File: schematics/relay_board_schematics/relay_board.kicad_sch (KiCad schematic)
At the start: 45 parts, among them J1 Programming Header, P1 ACT_PWR, P2 ACT_PWR, P3 ACTUATOR, Q1 MMBF170, Q2 MMBF170, SW1 SW_DIP_x04, U1 SPST_POWER_RELAY, U2 PIC16F1826-ISO, U3 dpdt_relay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

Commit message: first attempt at rerouting
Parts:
- D1: footprint Diode_SMD:D_SMB_Handsoldering -> Diode_THT:D_DO-35_SOD27_P7.62mm_Horizontal
- TP0, TP1, TP2, TP3: footprint TestPoint:TestPoint_Loop_D2.50mm_Drill1.0mm_LowProfile -> custom:Socket_Strip_Straight_1x01_Pitch2.54mm
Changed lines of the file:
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@@
     (property "Reference" "TP2" (id 0) (at 217.17 34.798 0))
     (property "Value" "TEST_1P" (id 1) (at 217.17 33.02 0))
-    (property "Footprint" "TestPoint:TestPoint_Loop_D2.50mm_Drill1.0mm_LowProfile" (id 2) (at 212.09 27.94 0)
+    (property "Footprint" "custom:Socket_Strip_Straight_1x01_Pitch2.54mm" (id 2) (at 212.09 27.94 0)
       (effects (font (size 1.27 1.27)) hide)
     )
@@
     (property "Reference" "TP1" (id 0) (at 203.2 34.798 0))
     (property "Value" "TEST_1P" (id 1) (at 203.2 33.02 0))
-    (property "Footprint" "TestPoint:TestPoint_Loop_D2.50mm_Drill1.0mm_LowProfile" (id 2) (at 198.12 27.94 0)
+    (property "Footprint" "custom:Socket_Strip_Straight_1x01_Pitch2.54mm" (id 2) (at 198.12 27.94 0)
       (effects (font (size 1.27 1.27)) hide)
     )
@@
     (property "Reference" "TP0" (id 0) (at 189.23 19.812 0))
     (property "Value" "TEST_1P" (id 1) (at 189.23 21.59 0))
-    (property "Footprint" "TestPoint:TestPoint_Loop_D2.50mm_Drill1.0mm_LowProfile" (id 2) (at 194.31 26.67 0)
+    (property "Footprint" "custom:Socket_Strip_Straight_1x01_Pitch2.54mm" (id 2) (at 194.31 26.67 0)
       (effects (font (size 1.27 1.27)) hide)
     )
@@
     (property "Reference" "D1" (id 0) (at 102.87 118.11 0))
     (property "Value" "D" (id 1) (at 97.79 118.11 0))
-    (property "Footprint" "Diode_SMD:D_SMB_Handsoldering" (id 2) (at 100.33 118.11 0)
+    (property "Footprint" "Diode_THT:D_DO-35_SOD27_P7.62mm_Horizontal" (id 2) (at 100.33 118.11 0)
       (effects (font (size 1.27 1.27)) hide)
     )
@@
     (property "Reference" "TP3" (id 0) (at 143.51 124.46 0))
     (property "Value" "TEST_1P" (id 1) (at 144.78 121.92 0))
-    (property "Footprint" "TestPoint:TestPoint_Loop_D2.50mm_Drill1.0mm_LowProfile" (id 2) (at 134.62 118.11 0)
+    (property "Footprint" "custom:Socket_Strip_Straight_1x01_Pitch2.54mm" (id 2) (at 134.62 118.11 0)
       (effects (font (size 1.27 1.27)) hide)
     )
@@
     )
     (path "/00000000-0000-0000-0000-00005dfd5087"
-      (reference "D1") (unit 1) (value "D") (footprint "Diode_SMD:D_SMB_Handsoldering")
+      (reference "D1") (unit 1) (value "D") (footprint "Diode_THT:D_DO-35_SOD27_P7.62mm_Horizontal")
     )
     (path "/00000000-0000-0000-0000-00005dfd508d"
@@
     )
     (path "/00000000-0000-0000-0000-0000597cb866"
-      (reference "TP0") (unit 1) (value "TEST_1P") (footprint "TestPoint:TestPoint_Loop_D2.50mm_Drill1.0mm_LowProfile")
+      (reference "TP0") (unit 1) (value "TEST_1P") (footprint "custom:Socket_Strip_Straight_1x01_Pitch2.54mm")
     )
     (path "/00000000-0000-0000-0000-0000597cb649"
-      (reference "TP1") (unit 1) (value "TEST_1P") (footprint "TestPoint:TestPoint_Loop_D2.50mm_Drill1.0mm_LowProfile")
+      (reference "TP1") (unit 1) (value "TEST_1P") (footprint "custom:Socket_Strip_Straight_1x01_Pitch2.54mm")
     )
     (path "/00000000-0000-0000-0000-0000597cb557"
-      (reference "TP2") (unit 1) (value "TEST_1P") (footprint "TestPoint:TestPoint_Loop_D2.50mm_Drill1.0mm_LowProfile")
+      (reference "TP2") (unit 1) (value "TEST_1P") (footprint "custom:Socket_Strip_Straight_1x01_Pitch2.54mm")
     )
     (path "/00000000-0000-0000-0000-00005e14f9f3"
-      (reference "TP3") (unit 1) (value "TEST_1P") (footprint "TestPoint:TestPoint_Loop_D2.50mm_Drill1.0mm_LowProfile")
+      (reference "TP3") (unit 1) (value "TEST_1P") (footprint "custom:Socket_Strip_Straight_1x01_Pitch2.54mm")
     )
     (path "/00000000-0000-0000-0000-00005dfd4fdd"

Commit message: addressed Jack's comments on pcb
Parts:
- D1: footprint Diode_THT:D_DO-35_SOD27_P7.62mm_Horizontal -> Diode_SMD:D_SMB_Handsoldering
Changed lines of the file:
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@@
     (property "Reference" "D1" (id 0) (at 102.87 118.11 0))
     (property "Value" "D" (id 1) (at 97.79 118.11 0))
-    (property "Footprint" "Diode_THT:D_DO-35_SOD27_P7.62mm_Horizontal" (id 2) (at 100.33 118.11 0)
+    (property "Footprint" "Diode_SMD:D_SMB_Handsoldering" (id 2) (at 100.33 118.11 0)
       (effects (font (size 1.27 1.27)) hide)
     )
@@
     )
     (path "/00000000-0000-0000-0000-00005dfd5087"
-      (reference "D1") (unit 1) (value "D") (footprint "Diode_THT:D_DO-35_SOD27_P7.62mm_Horizontal")
+      (reference "D1") (unit 1) (value "D") (footprint "Diode_SMD:D_SMB_Handsoldering")
     )
     (path "/00000000-0000-0000-0000-00005dfd508d"

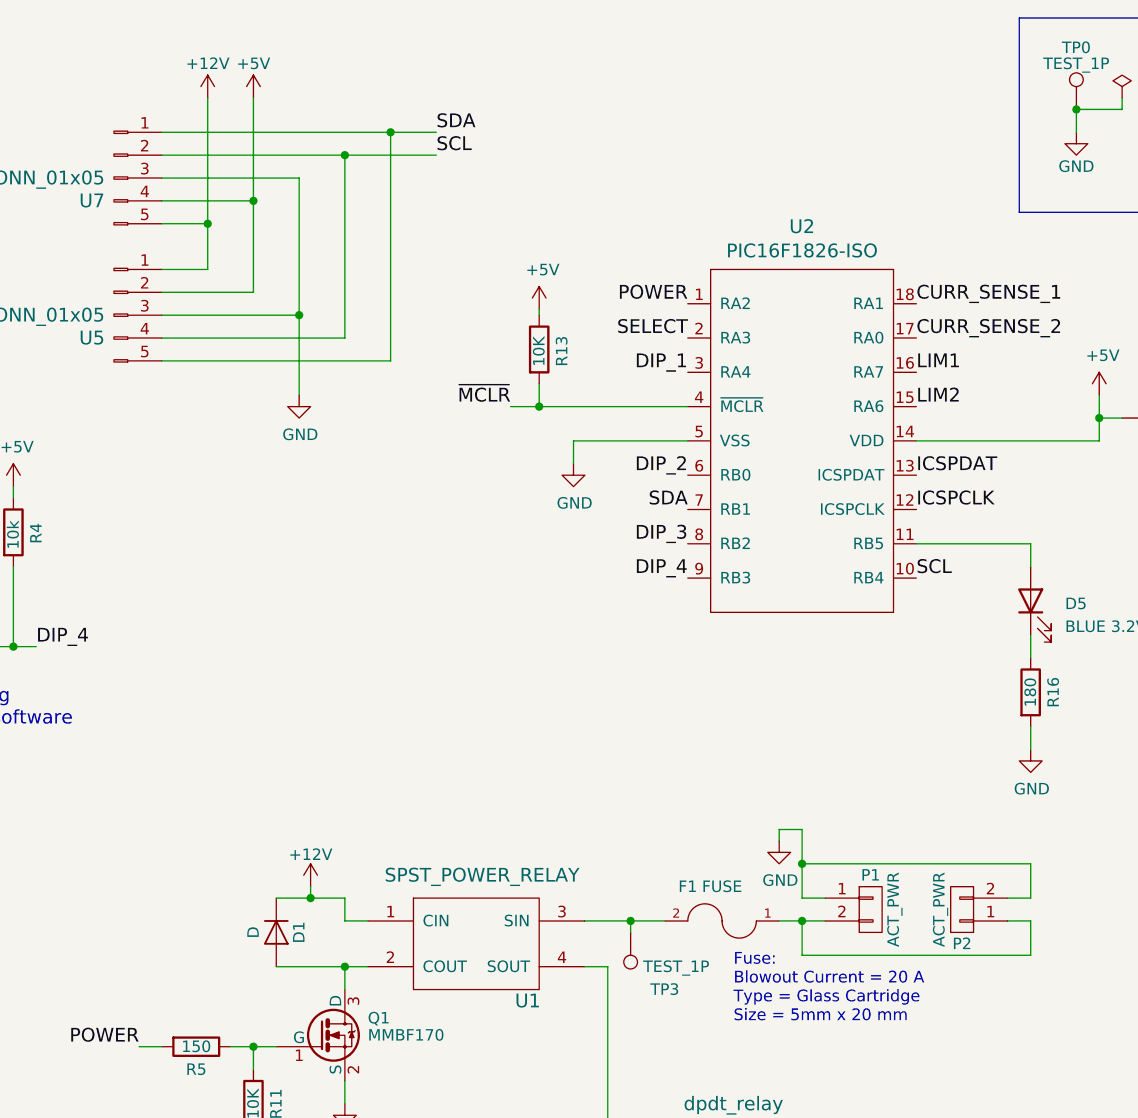
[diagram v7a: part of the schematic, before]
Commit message: Reversed the 5-pin and 2-pin screw terminals to match CAN support board
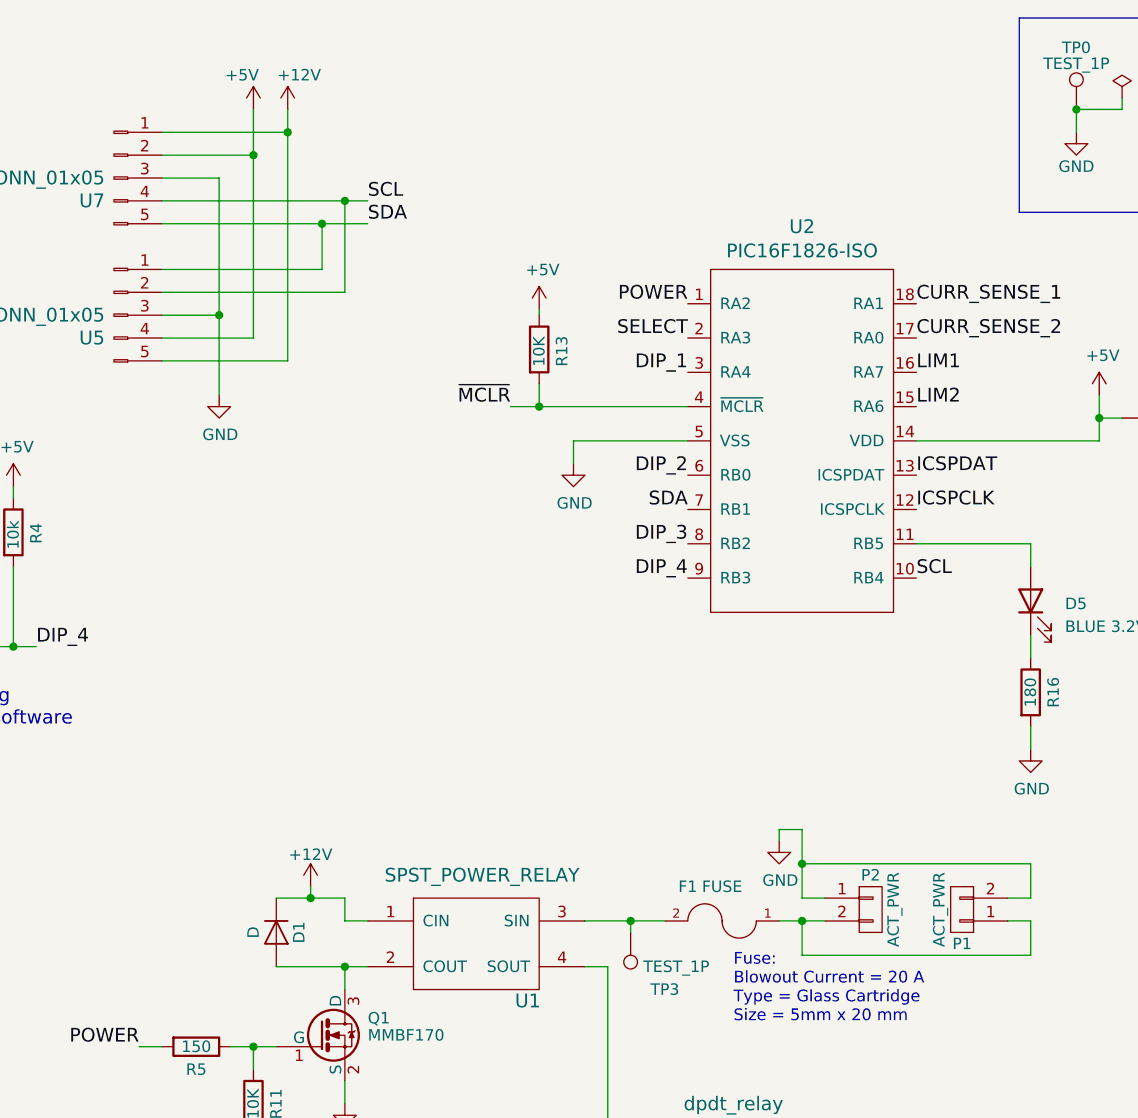
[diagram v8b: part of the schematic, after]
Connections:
- net +12V: now also U5.5, U7.1; no longer U5.1, U7.5
- net +5V: now also U5.4, U7.2; no longer U5.2, U7.4
- net GND: now also P1.2 (P2), P2.1 (P1); no longer P1.1 (P1), P2.2 (P2)
- net SCL: now also U5.2, U7.4; no longer U5.4, U7.2
- net SDA: now also U5.1, U7.5; no longer U5.5, U7.1
- new net: F1.1, P1.1 (P1), P2.2 (P2)
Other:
- moved on the sheet: P1, P2
